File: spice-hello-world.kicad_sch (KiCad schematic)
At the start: 5 parts

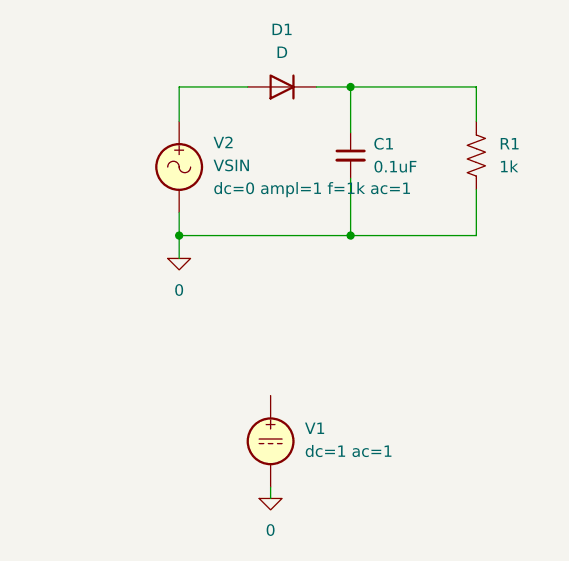
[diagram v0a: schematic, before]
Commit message: docs: enhance documentation with circuit screenshots
- Add schematic circuit diagram to README
- Include AC analysis (Bode plot) and transient analysis plots
- Update CLAUDE.md with image information
- Add screenshot directory with source files

🤖 Generated with [Claude Code](https://claude.ai/code)

Co-Authored-By: Claude <noreply@anthropic.com>
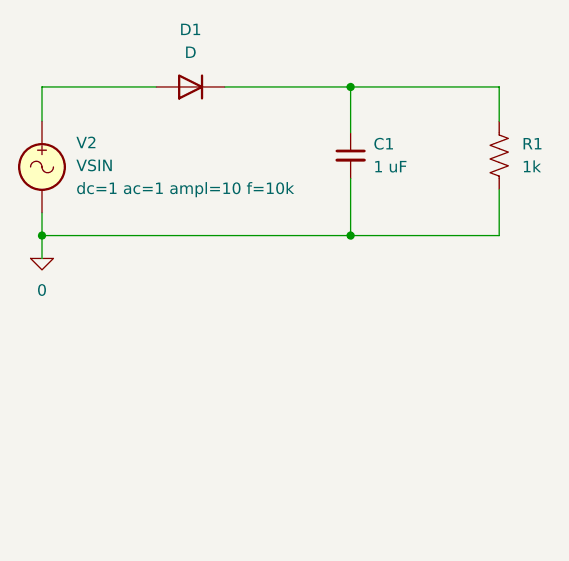
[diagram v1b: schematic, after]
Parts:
- removed V1: dc=1 ac=1, symbol Simulation_SPICE:VDC
- C1: value 0.1uF -> 1 uF
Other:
- moved on the sheet: D1, R1, V2
